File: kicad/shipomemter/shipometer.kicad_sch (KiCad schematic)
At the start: 24 parts, among them J101 Raspberry_Pi_40, J102 Conn_01x03, J104 ICM20948, J105 BME280, J106 ZED-F9R, U101 RaspberryPi 4B 2GB, U102 74LS138

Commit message: Imported BME280 stamp
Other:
- added sheet Pressure (BME280 stamp.kicad_sch)
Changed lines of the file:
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@@
+    )
+  )
+  (sheet (at 186.69 73.66) (size 16.51 7.62) (fields_autoplaced)
+    (stroke (width 0.1524) (type solid))
+    (fill (color 0 0 0 0.0000))
+    (property "Sheetname" "Pressure" (at 186.69 72.9484 0)
+      (effects (font (size 1.27 1.27)) (justify left bottom))
+    )
+    (property "Sheetfile" "BME280 stamp.kicad_sch" (at 186.69 81.8646 0)
+      (effects (font (size 1.27 1.27)) (justify left top))
+    )
+    (instances
+      (project "shipometer"
+        (path "/ba8024d5-8c9d-4001-9766-31acf13004f5" (page "5"))
+      )
     )
   )

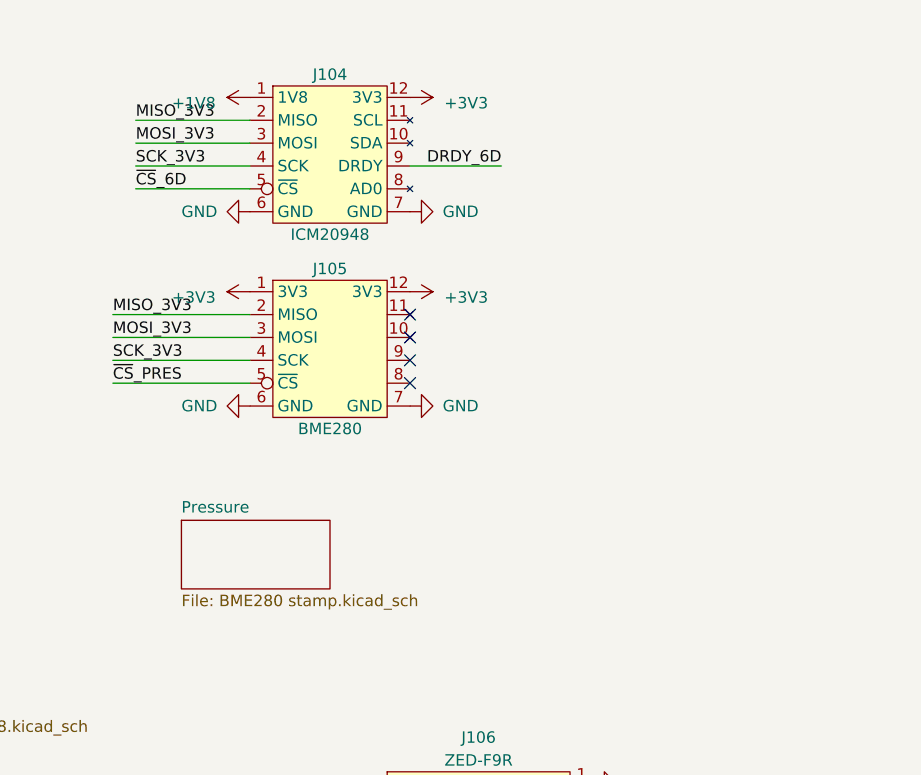
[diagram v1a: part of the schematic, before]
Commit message: Pulled in ICM20948
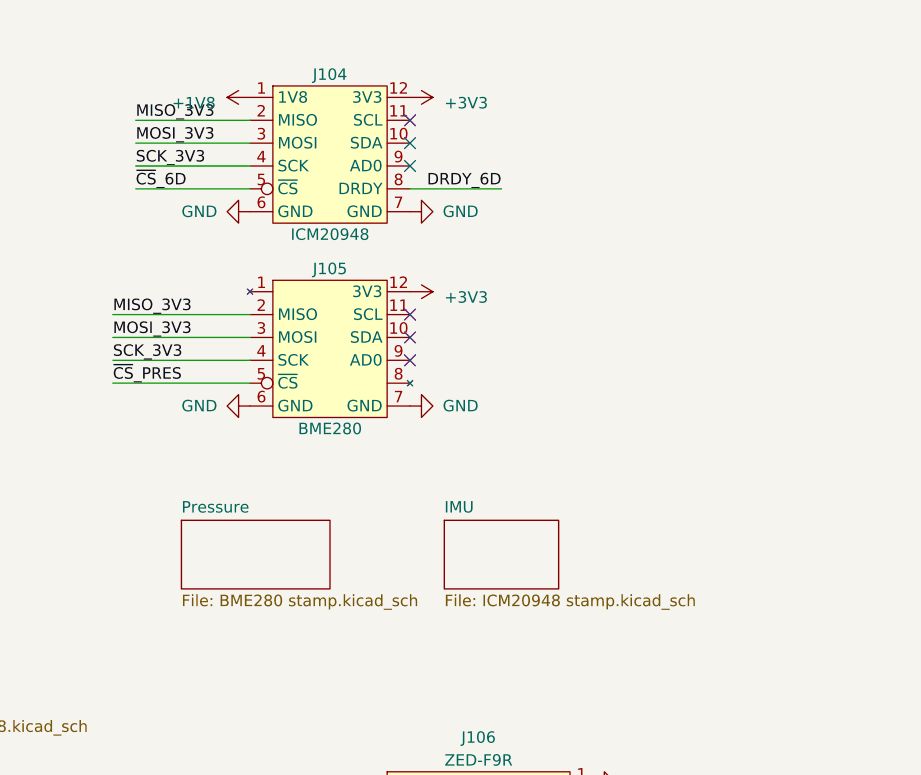
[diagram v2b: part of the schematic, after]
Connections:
- net +3V3: no longer J105.1 (3V3)
- net DRDY_6D: now also J104.8 (DRDY); no longer J104.9 (DRDY)
- no-connect marks 39 -> 41
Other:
- added sheet IMU (ICM20948 stamp.kicad_sch)
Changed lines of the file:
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@@
   (no_connect (at 232.41 110.49))
   (no_connect (at 43.18 66.04))
+  (no_connect (at 212.09 31.75))
   (no_connect (at 76.2 132.08))
   (no_connect (at 76.2 134.62))
@@
   (no_connect (at 232.41 120.65))
   (no_connect (at 229.87 142.24))
-  (no_connect (at 212.09 58.42))
   (no_connect (at 212.09 50.8))
   (no_connect (at 212.09 55.88))
   (no_connect (at 212.09 53.34))
+  (no_connect (at 212.09 34.29))
   (no_connect (at 232.41 118.11))
   (no_connect (at 207.01 110.49))
@@
   (no_connect (at 207.01 107.95))
   (no_connect (at 207.01 118.11))
+  (no_connect (at 212.09 29.21))
   (no_connect (at 152.4 128.27))
   (no_connect (at 152.4 130.81))
@@
     (stroke (width 0) (type default))
   )
-  (wire (pts (xy 212.09 34.29) (xy 222.25 34.29))
+  (wire (pts (xy 212.09 36.83) (xy 222.25 36.83))
     (stroke (width 0) (type default))
   )
@@
     (effects (font (size 1.27 1.27)) (justify left bottom))
   )
-  (label "DRDY_6D" (at 222.25 34.29 180) (fields_autoplaced)
+  (label "DRDY_6D" (at 222.25 36.83 180) (fields_autoplaced)
     (effects (font (size 1.27 1.27)) (justify right bottom))
   )
@@
         (path "/ba8024d5-8c9d-4001-9766-31acf13004f5"
           (reference "#PWR0126") (unit 1)
-        )
-      )
-    )
-  )
-  (symbol (lib_id "power:+3V3") (at 194.31 48.26 90) (unit 1)
-    (in_bom yes) (on_board yes) (dnp no) (fields_autoplaced)
-    (property "Reference" "#PWR0137" (at 198.12 48.26 0)
-      (effects (font (size 1.27 1.27)) hide)
-    )
-    (property "Value" "+3V3" (at 190.5 48.895 90)
-      (effects (font (size 1.27 1.27)) (justify left))
-    )
-    (property "Footprint" "" (at 194.31 48.26 0)
-      (effects (font (size 1.27 1.27)) hide)
-    )
-    (property "Datasheet" "" (at 194.31 48.26 0)
-      (effects (font (size 1.27 1.27)) hide)
-    )
-    (pin "1")
-    (instances
-      (project "shipometer"
-        (path "/ba8024d5-8c9d-4001-9766-31acf13004f5"
-          (reference "#PWR0137") (unit 1)
         )
       )
@@
     (instances
       (project "shipometer"
-        (path "/ba8024d5-8c9d-4001-9766-31acf13004f5" (page "5"))
-      )
-    )
+        (path "/ba8024d5-8c9d-4001-9766-31acf13004f5" (page "2"))
+      )
+    )
+  )
+  (sheet (at 215.9 73.66) (size 12.7 7.62) (fields_autoplaced)
+    (stroke (width 0.1524) (type solid))
+    (fill (color 0 0 0 0.0000))
+    (property "Sheetname" "IMU" (at 215.9 72.9484 0)
+      (effects (font (size 1.27 1.27)) (justify left bottom))
+    )
+    (property "Sheetfile" "ICM20948 stamp.kicad_sch" (at 215.9 81.8646 0)
+      (effects (font (size 1.27 1.27)) (justify left top))
+    )
+    (instances
+      (project "shipometer"
+        (path "/ba8024d5-8c9d-4001-9766-31acf13004f5" (page "3"))
+      )
+    )

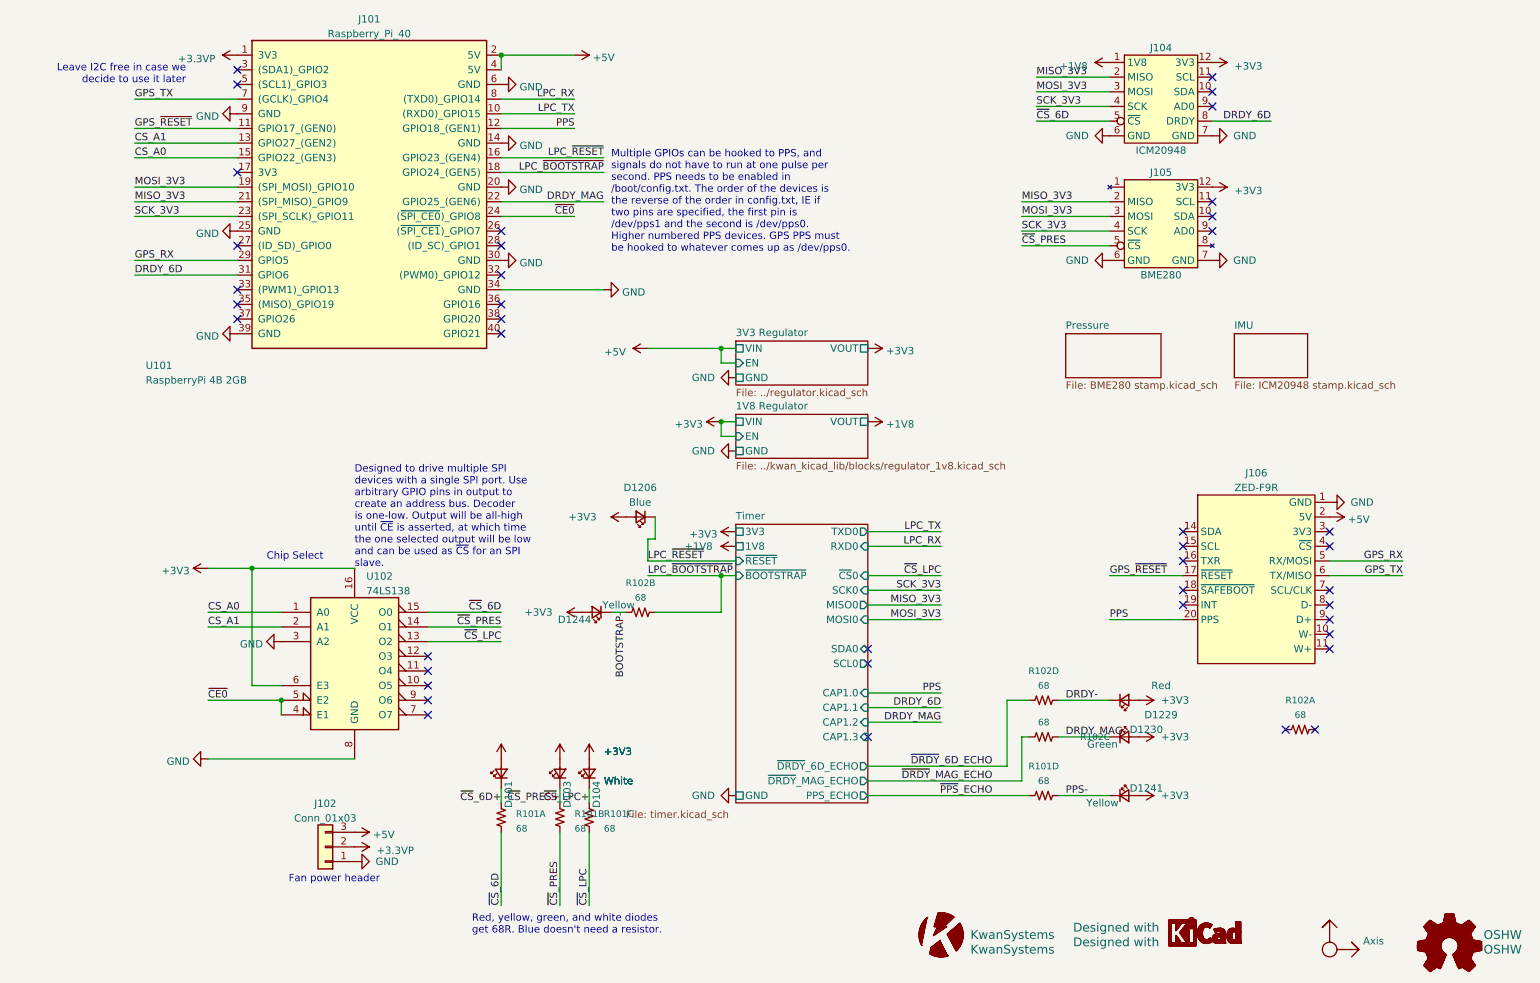
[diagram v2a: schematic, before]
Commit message: As ordered on 03 Apr 2023. Some but not all numbers-on-hand have been updated.
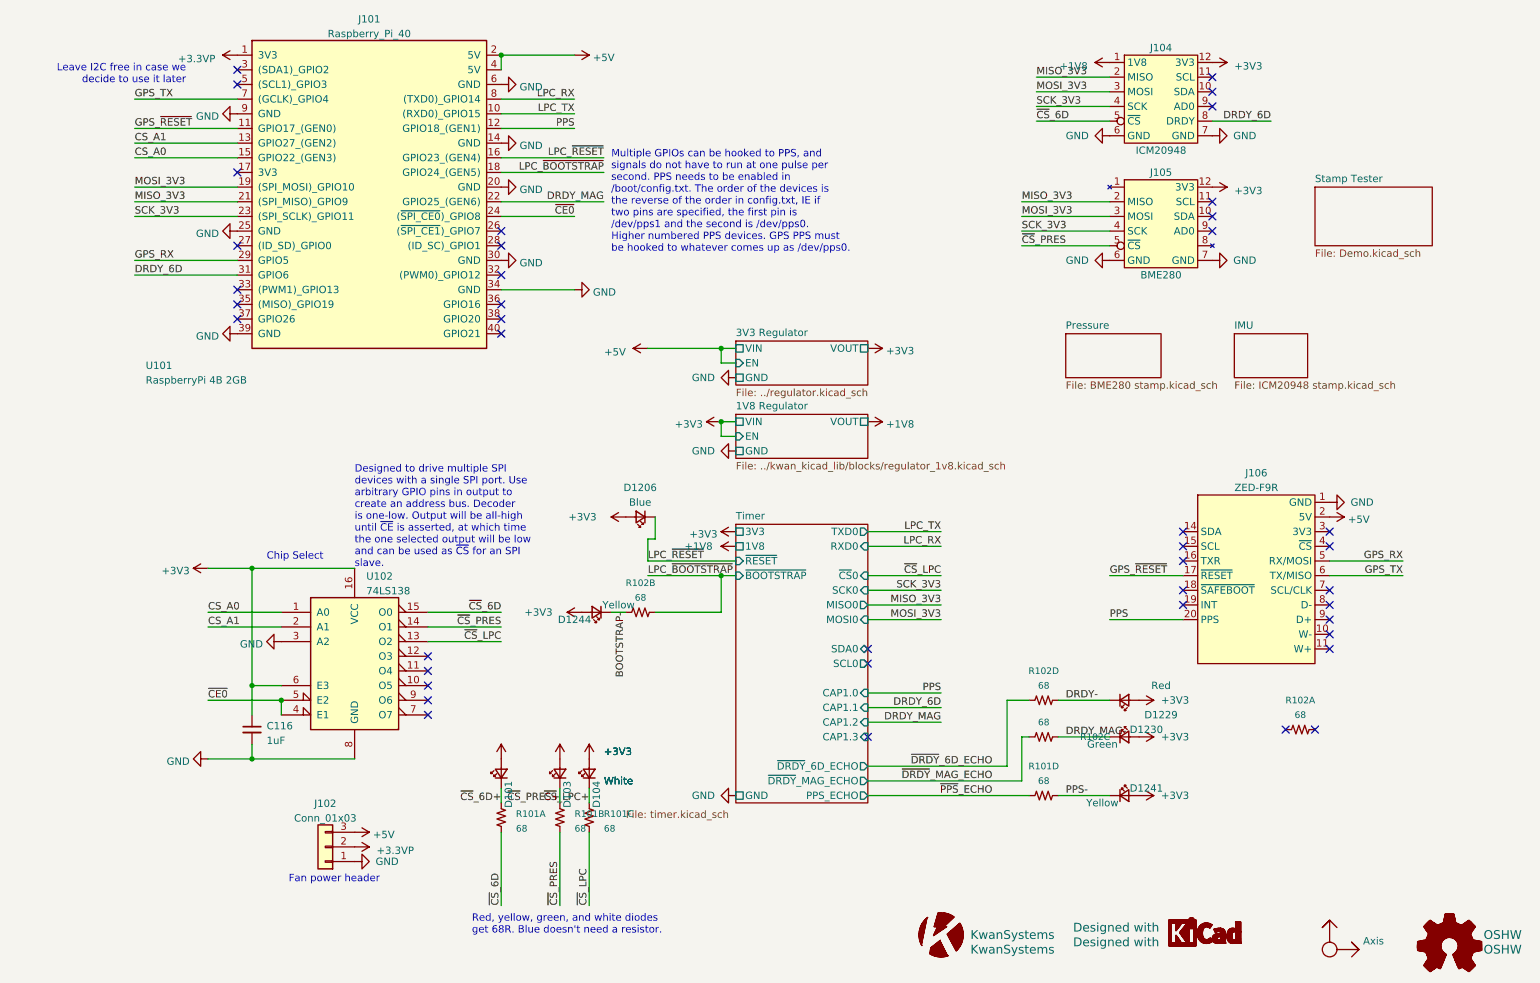
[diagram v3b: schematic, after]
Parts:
- added C116: 1uF, Capacitor_SMD:C_0603_1608Metric, symbol Device:C_Small
- D101, D103, D104: Number on hand 10 -> 6
- D1206: Number on hand 10 -> 9
- D1229: Number on hand 3+5 -> 2+2
- D1230: Number on hand 10 -> (none)
- D1241, D1244: Number on hand 10 -> 8
- J101: Number on hand 1 -> 0
- U102: Number on hand 4 -> 3
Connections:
- net +3V3: now also C116.1
- net GND: now also C116.2
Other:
- added sheet Stamp Tester (Demo.kicad_sch)
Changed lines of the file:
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@@
     (company "Kwan Systems")
   )
+  (junction (at 45.72 147.32) (diameter 0) (color 0 0 0 0)
+  )
   (junction (at 127 76.2) (diameter 0) (color 0 0 0 0)
   )
@@
   )
   (junction (at 50.8 137.16) (diameter 0) (color 0 0 0 0)
+  )
+  (junction (at 45.72 134.62) (diameter 0) (color 0 0 0 0)
   )
   (junction (at 127 115.57) (diameter 0) (color 0 0 0 0)
@@
     (stroke (width 0) (type default))
   )
-  (wire (pts (xy 38.1 147.32) (xy 63.5 147.32))
+  (wire (pts (xy 38.1 147.32) (xy 45.72 147.32))
     (stroke (width 0) (type default))
   )
@@
     (stroke (width 0) (type default))
   )
+  (wire (pts (xy 45.72 134.62) (xy 45.72 139.7))
+    (stroke (width 0) (type default))
+  )
   (wire (pts (xy 176.53 148.59) (xy 176.53 137.16))
     (stroke (width 0) (type default))
   )
-  (wire (pts (xy 88.9 66.04) (xy 106.68 66.04))
+  (wire (pts (xy 88.9 66.04) (xy 101.6 66.04))
     (stroke (width 0) (type default))
   )
@@
     (stroke (width 0) (type default))
   )
+  (wire (pts (xy 45.72 144.78) (xy 45.72 147.32))
+    (stroke (width 0) (type default))
+  )
   (wire (pts (xy 45.72 114.3) (xy 45.72 134.62))
     (stroke (width 0) (type default))
@@
   )
   (wire (pts (xy 127 76.2) (xy 127 78.74))
+    (stroke (width 0) (type default))
+  )
+  (wire (pts (xy 45.72 147.32) (xy 63.5 147.32))
     (stroke (width 0) (type default))
   )
@@
       (effects (font (size 1.27 1.27)) hide)
     )
-    (property "Number on hand" "10" (at 113.03 105.41 0)
+    (property "Number on hand" "9" (at 113.03 105.41 0)
       (effects (font (size 1.27 1.27)) hide)
     )
@@
     )
   )
-  (symbol (lib_id "power:GND") (at 106.68 66.04 90) (unit 1)
-    (in_bom yes) (on_board yes) (dnp no) (fields_autoplaced)
-    (property "Reference" "#PWR0106" (at 113.03 66.04 0)
-      (effects (font (size 1.27 1.27)) hide)
-    )
-    (property "Value" "GND" (at 109.855 66.4738 90)
-      (effects (font (size 1.27 1.27)) (justify right))
-    )
-    (property "Footprint" "" (at 106.68 66.04 0)
-      (effects (font (size 1.27 1.27)) hide)
-    )
-    (property "Datasheet" "" (at 106.68 66.04 0)
+  (symbol (lib_id "power:GND") (at 101.6 66.04 90) (unit 1)
+    (in_bom yes) (on_board yes) (dnp no) (fields_autoplaced)
+    (property "Reference" "#PWR0106" (at 107.95 66.04 0)
+      (effects (font (size 1.27 1.27)) hide)
+    )
+    (property "Value" "GND" (at 104.775 66.4738 90)
+      (effects (font (size 1.27 1.27)) (justify right))
+    )
+    (property "Footprint" "" (at 101.6 66.04 0)
+      (effects (font (size 1.27 1.27)) hide)
+    )
+    (property "Datasheet" "" (at 101.6 66.04 0)
       (effects (font (size 1.27 1.27)) hide)
     )
@@
         (path "/ba8024d5-8c9d-4001-9766-31acf13004f5"
           (reference "#PWR0106") (unit 1)
+        )
+      )
+    )
+  )
+  (symbol (lib_id "Device:C_Small") (at 45.72 142.24 0) (unit 1)
+    (in_bom yes) (on_board yes) (dnp no) (fields_autoplaced)
+    (property "Reference" "C116" (at 48.26 141.6113 0)
+      (effects (font (size 1.27 1.27)) (justify left))
+    )
+    (property "Value" "1uF" (at 48.26 144.1513 0)
+      (effects (font (size 1.27 1.27)) (justify left))
+    )
+    (property "Footprint" "Capacitor_SMD:C_0603_1608Metric" (at 45.72 142.24 0)
+      (effects (font (size 1.27 1.27)) hide)
+    )
+    (property "Datasheet" "https://connect.kemet.com:7667/gateway/IntelliData-ComponentDocumentation/1.0/download/datasheet/C0603C105K4PACTU" (at 45.72 142.24 0)
+      (effects (font (size 1.27 1.27)) hide)
+    )
+    (property "Digikey" "399-C0603C105K4PAC7411CT-ND" (at 45.72 142.24 0)
+      (effects (font (size 1.27 1.27)) hide)
+    )
+    (property "Mouser" "80-C0603C105K4PAC" (at 45.72 142.24 0)
+      (effects (font (size 1.27 1.27)) hide)
+    )
+    (pin "1")
+    (pin "2")
+    (instances
+      (project "shipometer"
+        (path "/ba8024d5-8c9d-4001-9766-31acf13004f5"
+          (reference "C116") (unit 1)
         )
       )
@@
       (effects (font (size 1.27 1.27)) hide)
     )
-    (property "Number on hand" "10" (at 99.06 149.86 0)
+    (property "Number on hand" "6" (at 99.06 149.86 0)
       (effects (font (size 1.27 1.27)) hide)
     )
@@
       (effects (font (size 1.27 1.27)) hide)
     )
-    (property "Number on hand" "10" (at 105.41 121.92 0)
+    (property "Number on hand" "8" (at 105.41 121.92 0)
       (effects (font (size 1.27 1.27)) hide)
     )
@@
       (effects (font (size 1.27 1.27)) hide)
     )
-    (property "Number on hand" "3+5" (at 196.85 137.16 0)
+    (property "Number on hand" "2+2" (at 196.85 137.16 0)
       (effects (font (size 1.27 1.27)) hide)
     )
@@
       (effects (font (size 1.27 1.27)) hide)
     )
-    (property "Number on hand" "10" (at 104.14 149.86 0)
+    (property "Number on hand" "6" (at 104.14 149.86 0)
       (effects (font (size 1.27 1.27)) hide)
     )
@@
       (effects (font (size 1.27 1.27)) hide)
     )
-    (property "Number on hand" "4" (at 63.5 129.54 0)
+    (property "Number on hand" "3" (at 63.5 129.54 0)
       (effects (font (size 1.27 1.27)) hide)
     )
@@
       (effects (font (size 1.27 1.27)) hide)
     )
-    (property "Number on hand" "1" (at 66.04 53.34 0)
+    (property "Number on hand" "0" (at 66.04 53.34 0)
       (effects (font (size 1.27 1.27)) hide)
     )
@@
       (effects (font (size 1.27 1.27)) hide)
     )
-    (property "Number on hand" "10" (at 196.85 153.67 0)
+    (property "Number on hand" "8" (at 196.85 153.67 0)
       (effects (font (size 1.27 1.27)) hide)
     )
@@
       (effects (font (size 1.27 1.27)) hide)
     )
-    (property "Number on hand" "10" (at 196.85 143.51 0)
+    (property "Number on hand" "" (at 196.85 143.51 0)
       (effects (font (size 1.27 1.27)) hide)
     )
@@
       (effects (font (size 1.27 1.27)) hide)
     )
-    (property "Number on hand" "10" (at 88.9 149.86 0)
+    (property "Number on hand" "6" (at 88.9 149.86 0)
       (effects (font (size 1.27 1.27)) hide)
     )
@@
     (instances
       (project "shipometer"
-        (path "/ba8024d5-8c9d-4001-9766-31acf13004f5" (page "12"))
+        (path "/ba8024d5-8c9d-4001-9766-31acf13004f5" (page "6"))
       )
     )
@@
       )
     )
+  )
+  (sheet (at 229.87 48.26) (size 20.32 10.16) (fields_autoplaced)
+    (stroke (width 0.1524) (type solid))
+    (fill (color 0 0 0 0.0000))
+    (property "Sheetname" "Stamp Tester" (at 229.87 47.5484 0)
+      (effects (font (size 1.27 1.27)) (justify left bottom))
+    )
+    (property "Sheetfile" "Demo.kicad_sch" (at 229.87 59.0046 0)
+      (effects (font (size 1.27 1.27)) (justify left top))
+    )
+    (instances
+      (project "shipometer"
+        (path "/ba8024d5-8c9d-4001-9766-31acf13004f5" (page "7"))
+      )
+    )
